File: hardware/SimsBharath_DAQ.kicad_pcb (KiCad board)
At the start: 2 copper layers, 74 x 119 mm, 109 parts, among them J1 Conn_02x05_Odd_Even, J10 702471052, J11 702471052, J12 Conn_01x03, J2 USB1030-GF-P-B-B, J3 702471052, J4 702471052, J5 702471052, J6 702471052, J7 702471052, J8 702471052, J9 1-406507-5, SW1 SW_Push, U1 STM32H753ZIT6, U2 MIC37100-3.3WS, U3 LAN8742A-CZ-TR, U4 H1102NL, X1 XRCGB25M000F3A16R0, X2 XRCGB25M000F3A16R0, X3 CM7V-T1A-32.768KHZ-7PF-20PPM-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

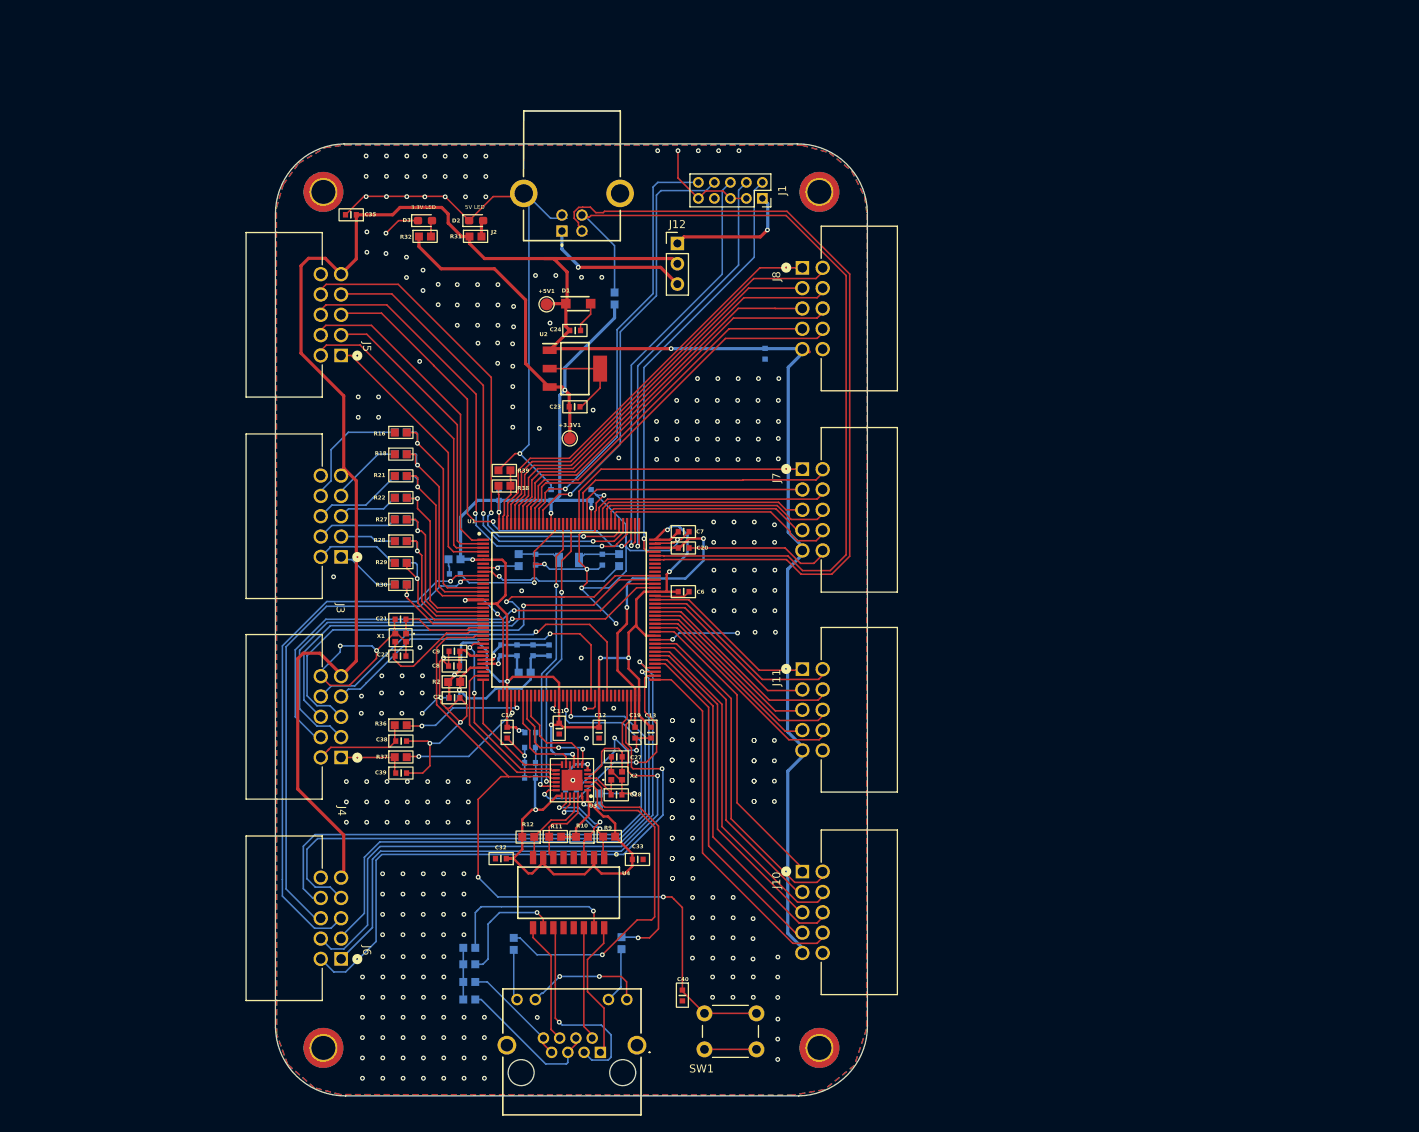
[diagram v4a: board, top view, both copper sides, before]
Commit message: changed header spacing
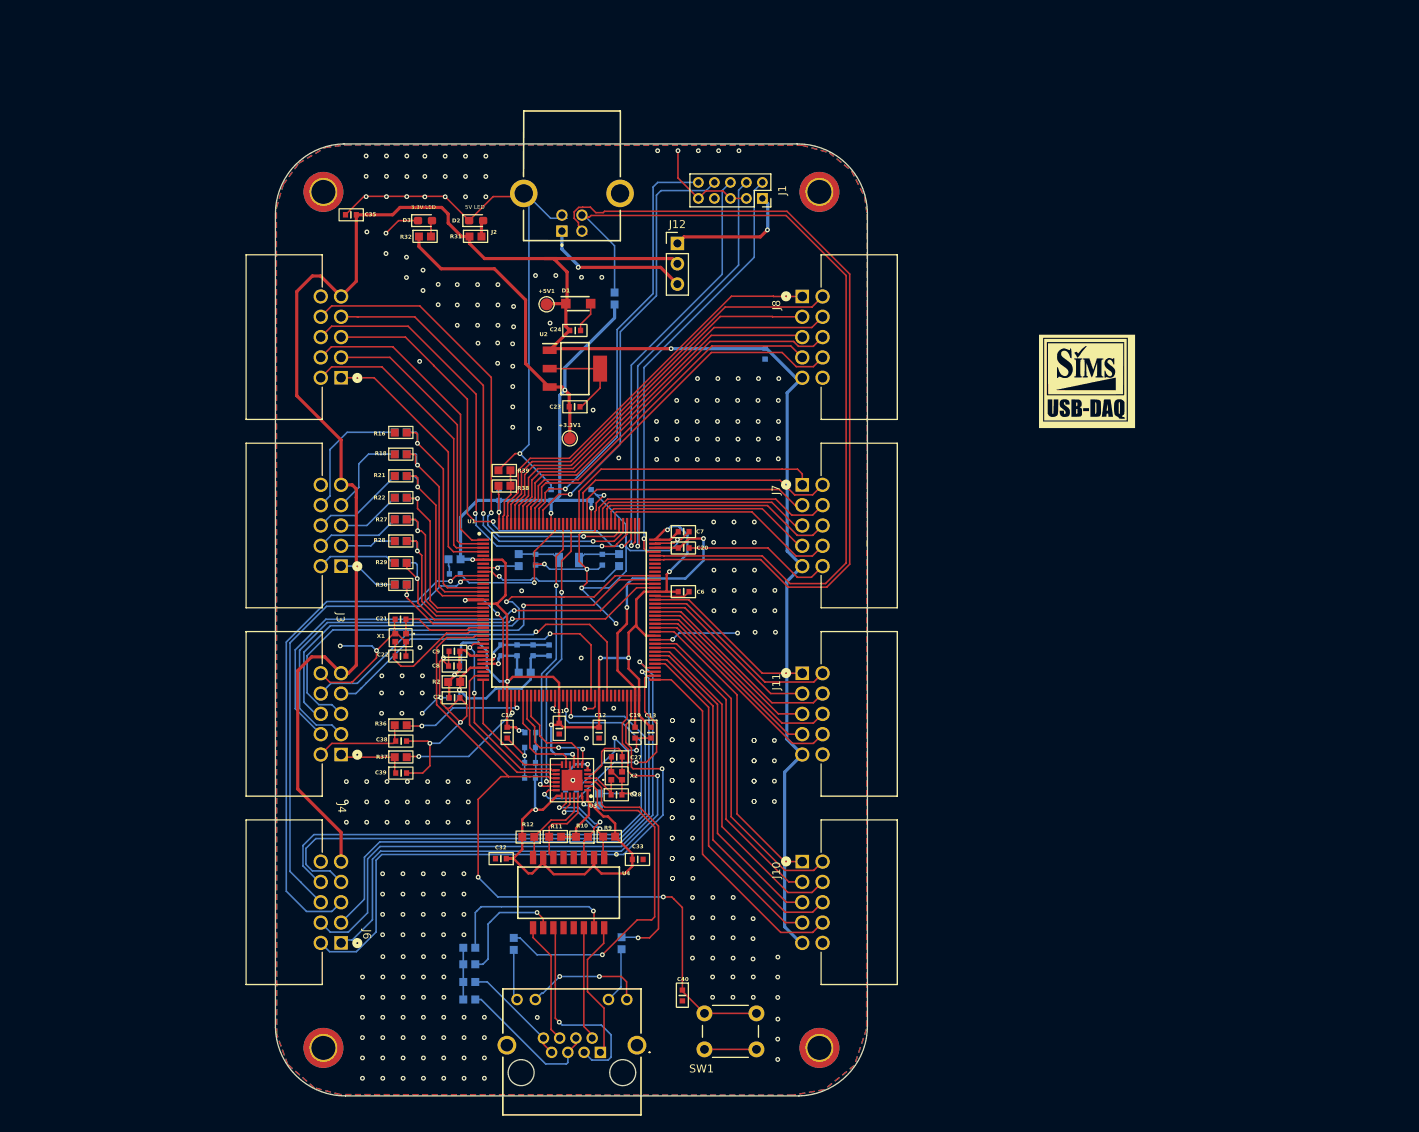
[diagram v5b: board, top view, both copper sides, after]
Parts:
- added G***: LOGO, LOGO, F.Cu at (195.4, 67.2)
- moved J8 3.58 mm to (159.8, 56.6)
- moved J5 2.79 mm to (102.2, 66.8)
- moved J6 2.00 mm to (102.2, 137.4)
- moved J7 1.96 mm to (159.8, 80.1)
- moved J10 1.26 mm to (159.8, 127.2)
- moved J3 1.16 mm to (102.2, 90.3)
- moved J11 0.51 mm to (159.8, 103.7)
- moved J4 0.37 mm to (102.2, 113.9)
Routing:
- net +5V: track 282.5 -> 275.5 mm
- net GND: track 382.2 -> 377.5 mm, vias 316 -> 305
- net /CONNECTORS/I2C1_SCL: track 64.2 -> 61.4 mm
- net /CONNECTORS/I2C2_SCL: track 74.4 -> 72.1 mm
- net /CONNECTORS/PB3: track 53.4 -> 51.3 mm
- net /CONNECTORS/PB1: track 55.7 -> 53.7 mm
- net /CONNECTORS/UART2_TX: track 69.0 -> 67.0 mm
- net /CONNECTORS/PB0: track 53.8 -> 51.8 mm
- net /CONNECTORS/PB2: track 51.5 -> 49.5 mm
- net /CONNECTORS/UART1_RX: track 76.8 -> 74.8 mm
- net /CONNECTORS/I2C1_SDA: track 69.5 -> 67.6 mm
- net /CONNECTORS/USB_FS_D P: track 106.7 -> 108.7 mm
- net /CONNECTORS/USB_FS_D N: track 103.1 -> 105.0 mm
- net /CONNECTORS/ADC3_2: track 9.22 -> 11.1 mm
- net /CONNECTORS/PB4: track 49.1 -> 47.3 mm
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
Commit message: Final Updated design
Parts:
- added R40: 10k, Murata:RESC1608X95N, B.Cu at (126.6, 79.4)
- G***: moved to B.Cu
- moved G*** 64.0 mm to (131.4, 65.6), turned to 180 degrees
- renumbered J9 to J11, J6 to J3, J3 to J5, J5 to J6, J8 to J7, J7 to J8, J11 to J9
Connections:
- J4 pad 7: /CONNECTORS/PWM10 -> /CONNECTORS/PWM4
- J4 pad 8: /CONNECTORS/PWM11 -> /CONNECTORS/PWM5
- U1 pad 111: /CONNECTORS/SPI5_MOSI -> /CONNECTORS/SPI5_SCK
- U1 pad 113: /CONNECTORS/SPI5_NSS -> /CONNECTORS/SPI5_MOSI
- U1 pad 114: /CONNECTORS/SPI5_SCK -> /CONNECTORS/SPI5_NSS
- U1 pad 132: unconnected-(U1-PG15-Pad132) -> /CONNECTORS/PB7
- U1 pad 135: /CONNECTORS/PB7 -> /CONNECTORS/PB6
- U1 pad 136: /CONNECTORS/PB6 -> /CONNECTORS/PB5
- U1 pad 137: /CONNECTORS/PB5 -> /CONNECTORS/PB4
- U1 pad 138: /CONNECTORS/PB4 -> Net-(U1-BOOT0)
- U1 pad 2: /CONNECTORS/SPI4_NSS -> unconnected-(U1-PE3-Pad2)
- U1 pad 3: /CONNECTORS/SPI4_MISO -> /CONNECTORS/SPI4_NSS
- U1 pad 34: unconnected-(U1-PA0-WKUP-Pad34) -> /CONNECTORS/PWM5
- U1 pad 37: unconnected-(U1-PA3-Pad37) -> /CONNECTORS/PWM4
- U1 pad 4: /CONNECTORS/SPI4_MOSI -> /CONNECTORS/SPI4_MISO
- U1 pad 42: unconnected-(U1-PA6-Pad42) -> /CONNECTORS/PWM3
- U1 pad 5: unconnected-(U1-PE6-Pad5) -> /CONNECTORS/SPI4_MOSI
- U1 pad 60: /CONNECTORS/PWM10 -> /CONNECTORS/PWM2
- U1 pad 64: /CONNECTORS/PWM11 -> unconnected-(U1-PE11-Pad64)
- U1 pad 96: /CONNECTORS/PWM0 -> /CONNECTORS/PWM1
- U1 pad 97: /CONNECTORS/PWM1 -> /CONNECTORS/PWM0
- U1 pad 98: /CONNECTORS/PWM2 -> unconnected-(U1-PC8-Pad98)
- U1 pad 99: /CONNECTORS/PWM3 -> unconnected-(U1-PC9-Pad99)
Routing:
- net /CONNECTORS/PWM11: track 47.1 -> 0.00 mm, vias 1 -> 0
- net /CONNECTORS/PWM10: track 41.5 -> 0.00 mm, vias 1 -> 0
- net /CONNECTORS/PWM3: track 60.7 -> 33.6 mm
- net /CONNECTORS/PWM4: track 0.00 -> 22.5 mm, vias 0 -> 1
- net /CONNECTORS/PWM5: track 0.00 -> 21.4 mm, vias 0 -> 1
- net unconnected-(U1-PE11-Pad64): track 0.00 -> 17.5 mm, vias 0 -> 1
- net Net-(U1-BOOT0): track 0.00 -> 5.70 mm, vias 0 -> 1
- net /CONNECTORS/PWM2: track 58.9 -> 54.6 mm
- net /CONNECTORS/PWM0: track 61.5 -> 65.0 mm
- net /CONNECTORS/SPI5_SCK: track 62.5 -> 65.5 mm
- net /CONNECTORS/PB7: track 48.2 -> 45.9 mm
- net /CONNECTORS/PB4: track 47.3 -> 45.3 mm
- net /CONNECTORS/PB5: track 49.5 -> 47.6 mm
- net /CONNECTORS/PB6: track 46.2 -> 44.3 mm
- net /CONNECTORS/SPI5_MOSI: track 58.0 -> 56.2 mm
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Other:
- board text added: "5V J"
- board text added: "5V U"
- board text added: "ADC"
- board text added: "DAC & PWM"
- board text added: "GPIO P0"
- board text added: "GPIO P1"
- board text added: "GPIO P2"
- board text added: "GPIO P3"
- board text added: "J11"
- board text added: "J6"
- board text added: "JTAG"
- board text added: "SPI"
- board text added: "SiMS USB-DAQ"
- board text added: "UART & I2C"

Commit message: final submission
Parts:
- moved C9 0.06 mm to (116.3, 101.0)
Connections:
- C15 pad 2: GNDA -> GND
- C16 pad 2: GNDA -> GND
- C17 pad 2: GNDA -> GND
- C18 pad 2: GNDA -> GND
- U1 pad 31: GNDA -> GND
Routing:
- net GND: track 376.5 -> 431.8 mm, vias 303 -> 306
- net GNDA: track 9.47 -> 0.00 mm, vias 1 -> 0
- net /CONNECTORS/USB_FS_D P: track 108.7 -> 110.0 mm
- net /CONNECTORS/USB_FS_D N: track 105.0 -> 104.2 mm
- net +3.3V: track 237.7 -> 236.9 mm
- net Net-(J11-Pad4): track 18.5 -> 17.8 mm
- net /CONNECTORS/RX P: track 26.0 -> 26.6 mm

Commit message: final update
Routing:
- net +3.3V: track 236.9 -> 234.0 mm, vias 14 -> 15
- net /CONNECTORS/SPI4_MOSI: track 33.9 -> 32.9 mm
- net /CONNECTORS/SPI4_MISO: track 38.2 -> 37.3 mm
- net /CONNECTORS/SPI4_NSS: track 36.1 -> 35.3 mm
- net /CONNECTORS/USB_FS_D N: track 104.2 -> 104.9 mm
- net +5V: track 275.5 -> 276.1 mm
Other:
- board text added: "+5V"
- board text added: "GND"
- board text added: "JTCK"
- board text added: "JTDI"
- board text added: "JTDO"
- board text added: "JTMS"
- board text added: "~{JRST}"
